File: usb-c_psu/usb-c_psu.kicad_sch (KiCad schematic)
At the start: 50 parts, among them J1 Conn_01x01_Socket, J10 Conn_01x01_Socket, J11 Screw_Terminal_01x02, J12 Conn_01x04, J2 Conn_01x01_Socket, J3 Conn_01x01_Socket, J4 Conn_01x01_Socket, J5 Conn_01x01_Socket, J6 Conn_01x01_Socket, J7 Conn_01x01_Socket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

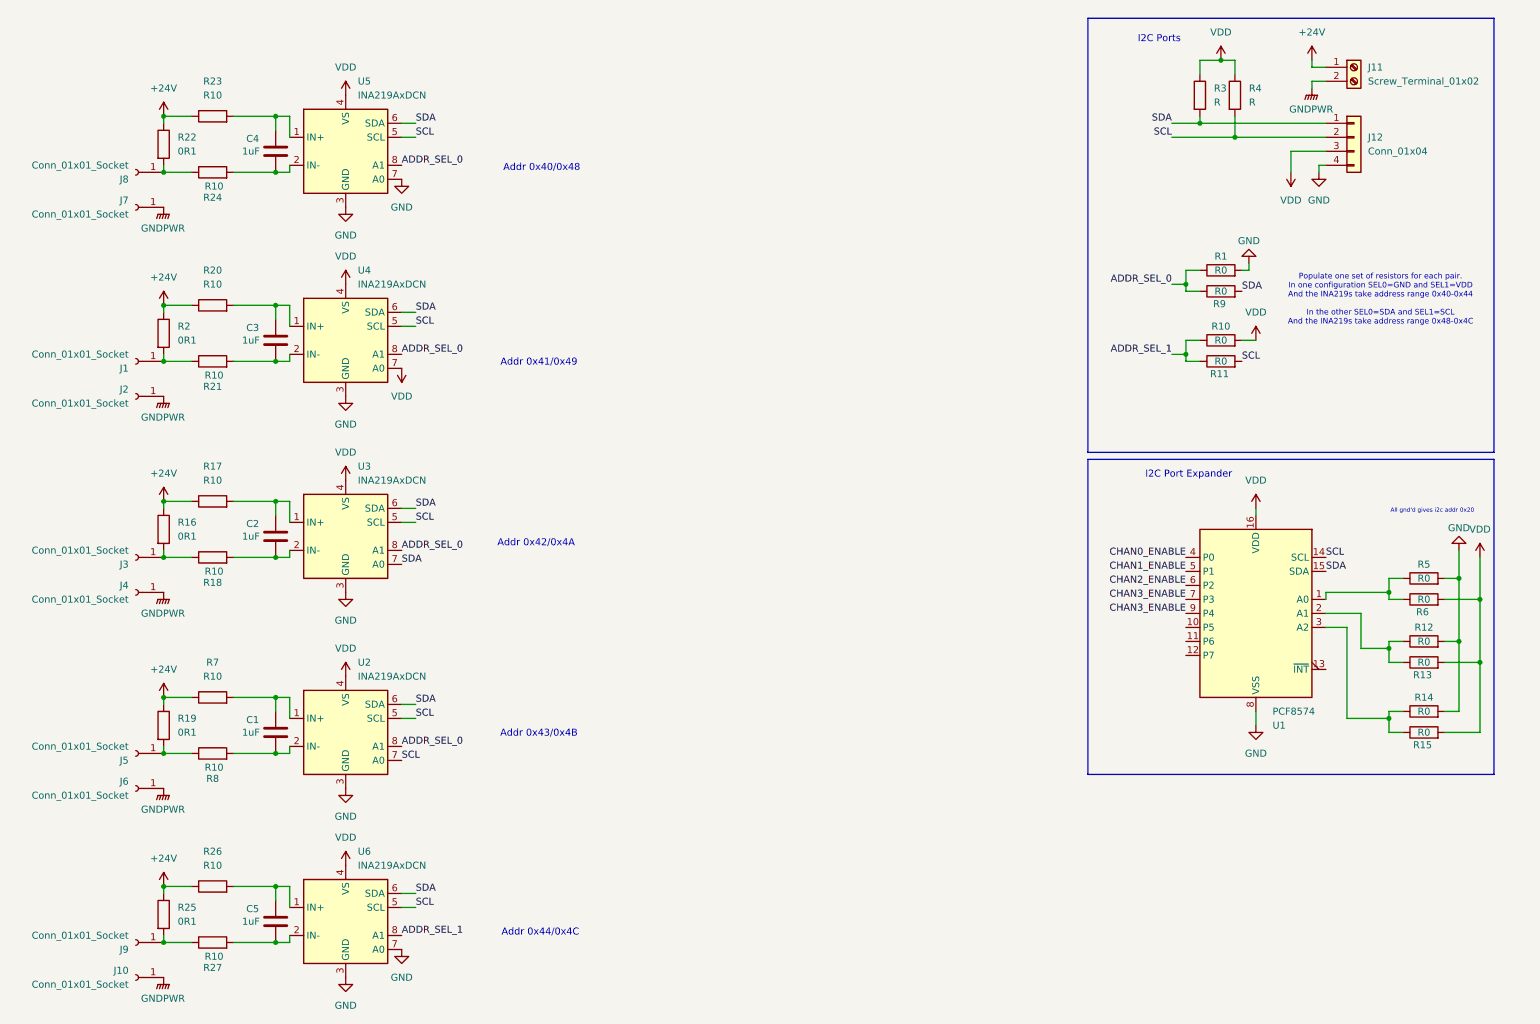
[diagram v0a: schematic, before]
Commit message: update connector footprints
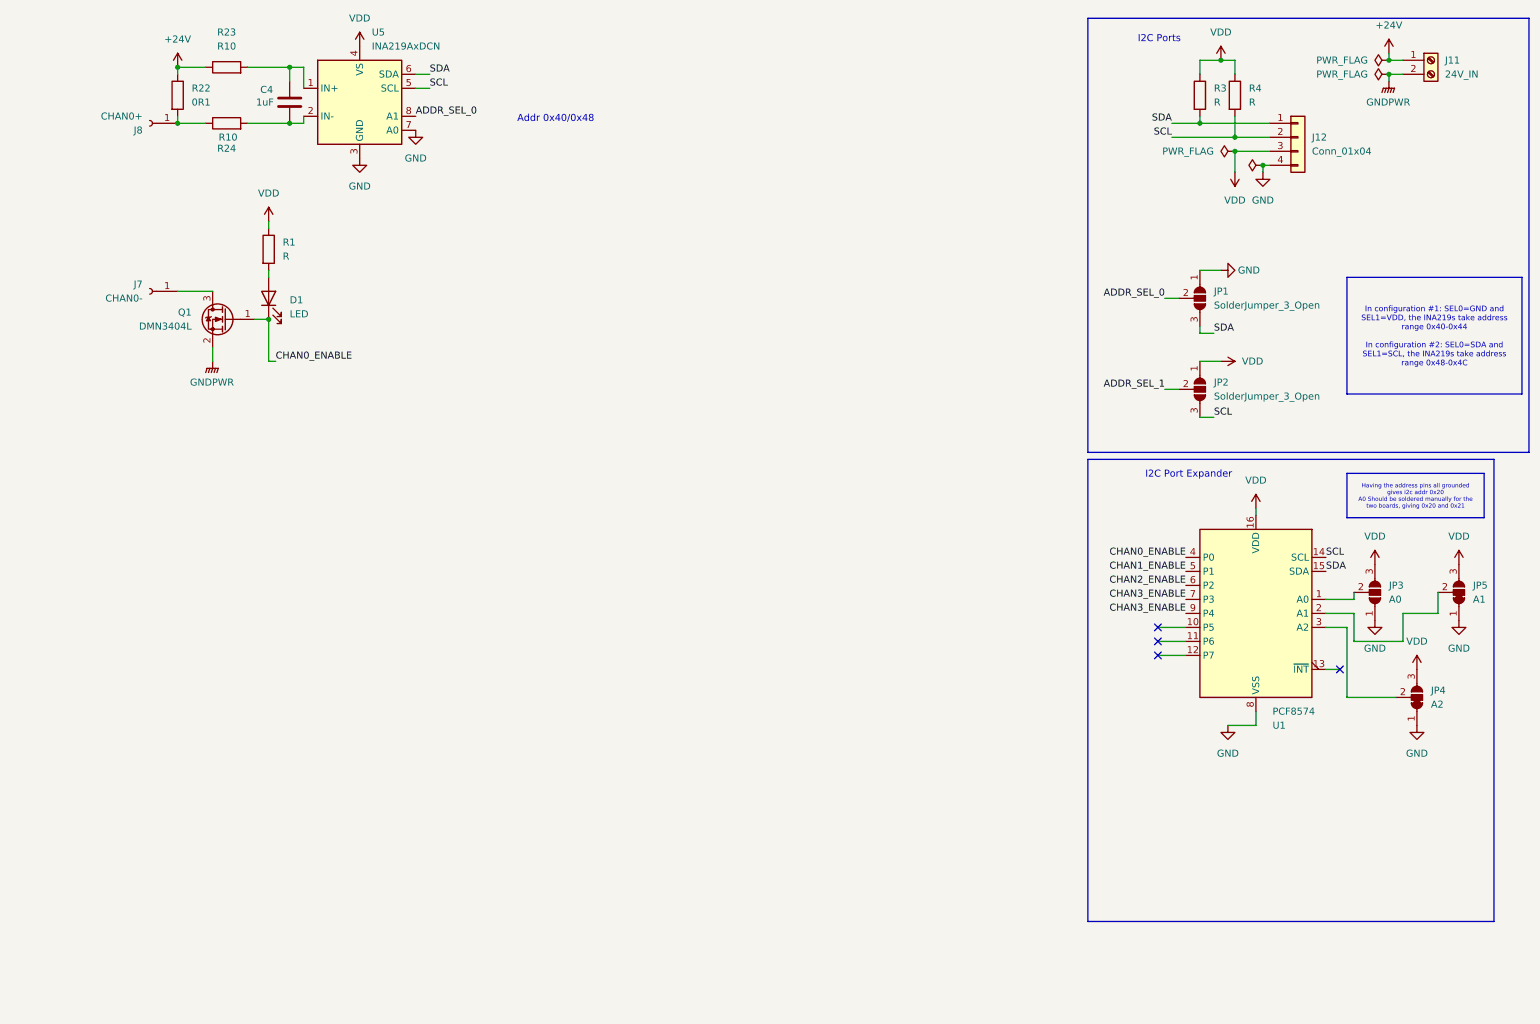
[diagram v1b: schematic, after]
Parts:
- removed C1, C2, C3, C5: 1uF, symbol Device:C
- removed J1, J10, J2, J3, J4, J5, J6, J9: Conn_01x01_Socket, Connector_Wire:SolderWire-0.5sqmm_1x01_D0.9mm_OD2.1mm, symbol Connector:Conn_01x01_Socket
- removed R10, R11, R12, R13, R14, R15, R5, R6, R9: R0, Resistor_SMD:R_0402_1005Metric_Pad0.72x0.64mm_HandSolder, symbol Device:R
- removed R16, R19, R2, R25: 0R1, Resistor_SMD:R_1210_3225Metric_Pad1.30x2.65mm_HandSolder, symbol Device:R
- removed R17, R18, R20, R21, R26, R27, R7, R8: R10, symbol Device:R
- removed U2, U3, U4, U6: INA219AxDCN, Package_TO_SOT_SMD:SOT-23-8, symbol Sensor_Energy:INA219AxDCN
- added D1: LED, LED_SMD:LED_0402_1005Metric, symbol Device:LED
- added JP1, JP2: SolderJumper_3_Open, Jumper:SolderJumper-3_P1.3mm_Open_RoundedPad1.0x1.5mm_NumberLabels, symbol Jumper:SolderJumper_3_Open
- added JP3: A0, Jumper:SolderJumper-3_P1.3mm_Open_RoundedPad1.0x1.5mm_NumberLabels, symbol Jumper:SolderJumper_3_Open
- added JP4: A2, Jumper:SolderJumper-3_P1.3mm_Bridged12_Pad1.0x1.5mm_NumberLabels, symbol Jumper:SolderJumper_3_Bridged12
- added JP5: A1, Jumper:SolderJumper-3_P1.3mm_Bridged12_Pad1.0x1.5mm_NumberLabels, symbol Jumper:SolderJumper_3_Bridged12
- added Q1: DMN3404L, Package_TO_SOT_SMD:SOT-23, symbol Transistor_FET:DMN3404L
- C4: footprint (none) -> Capacitor_SMD:C_0603_1608Metric
- J11: value Screw_Terminal_01x02 -> 24V_IN
- J7: value Conn_01x01_Socket -> CHAN0-
- J8: value Conn_01x01_Socket -> CHAN0+
- R1: value R0 -> R; footprint Resistor_SMD:R_0402_1005Metric_Pad0.72x0.64mm_HandSolder -> (none)
- R23, R24: footprint (none) -> Resistor_SMD:R_0402_1005Metric
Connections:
- net ADDR_SEL_0: now also JP1.2 (C); no longer R1.1
- net ADDR_SEL_1: now also JP2.2 (C)
- net CHAN0_ENABLE: now also D1.1 (K), Q1.1 (G)
- net GND: now also JP1.1 (A), JP3.1 (A), JP4.1 (A), JP5.1 (A); no longer R1.2
- net GNDPWR: now also Q1.2 (S); no longer J7.1 (Pin_1)
- net SCL: now also JP2.3 (B)
- net SDA: now also JP1.3 (B)
- net VDD: now also R1.1, JP2.1 (A), JP3.3 (B), JP4.3 (B), JP5.3 (B)
- net at U1.1 (A0): now also JP3.2 (C)
- net at U1.2 (A1): now also JP5.2 (C)
- net at U1.3 (A2): now also JP4.2 (C)
- new net: D1.2 (A), R1.2
- new net: J7.1 (Pin_1), Q1.3 (D)
- no-connect marks 0 -> 4
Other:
- note removed: "Addr 0x41/0x49"
- note removed: "Addr 0x42/0x4A"
- note removed: "Addr 0x43/0x4B"
- note removed: "Addr 0x44/0x4C"
- note removed: "All gnd'd gives i2c addr 0x20"
- note removed: "Populate one set of resistors for each pair. In one configuration SEL0=GND and SEL1=VDD And the INA219s take address range 0x40-0x44 In the other SEL0=SDA and SEL1=SCL And the INA219s take address range 0x48-0x4C"
- title: (none) -> 5x USB-C PSU Carrier Board
- moved on the sheet: C4, J11, J12, J7, J8, R22, R23, R24, U5
